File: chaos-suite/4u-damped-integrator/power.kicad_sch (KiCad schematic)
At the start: 14 parts

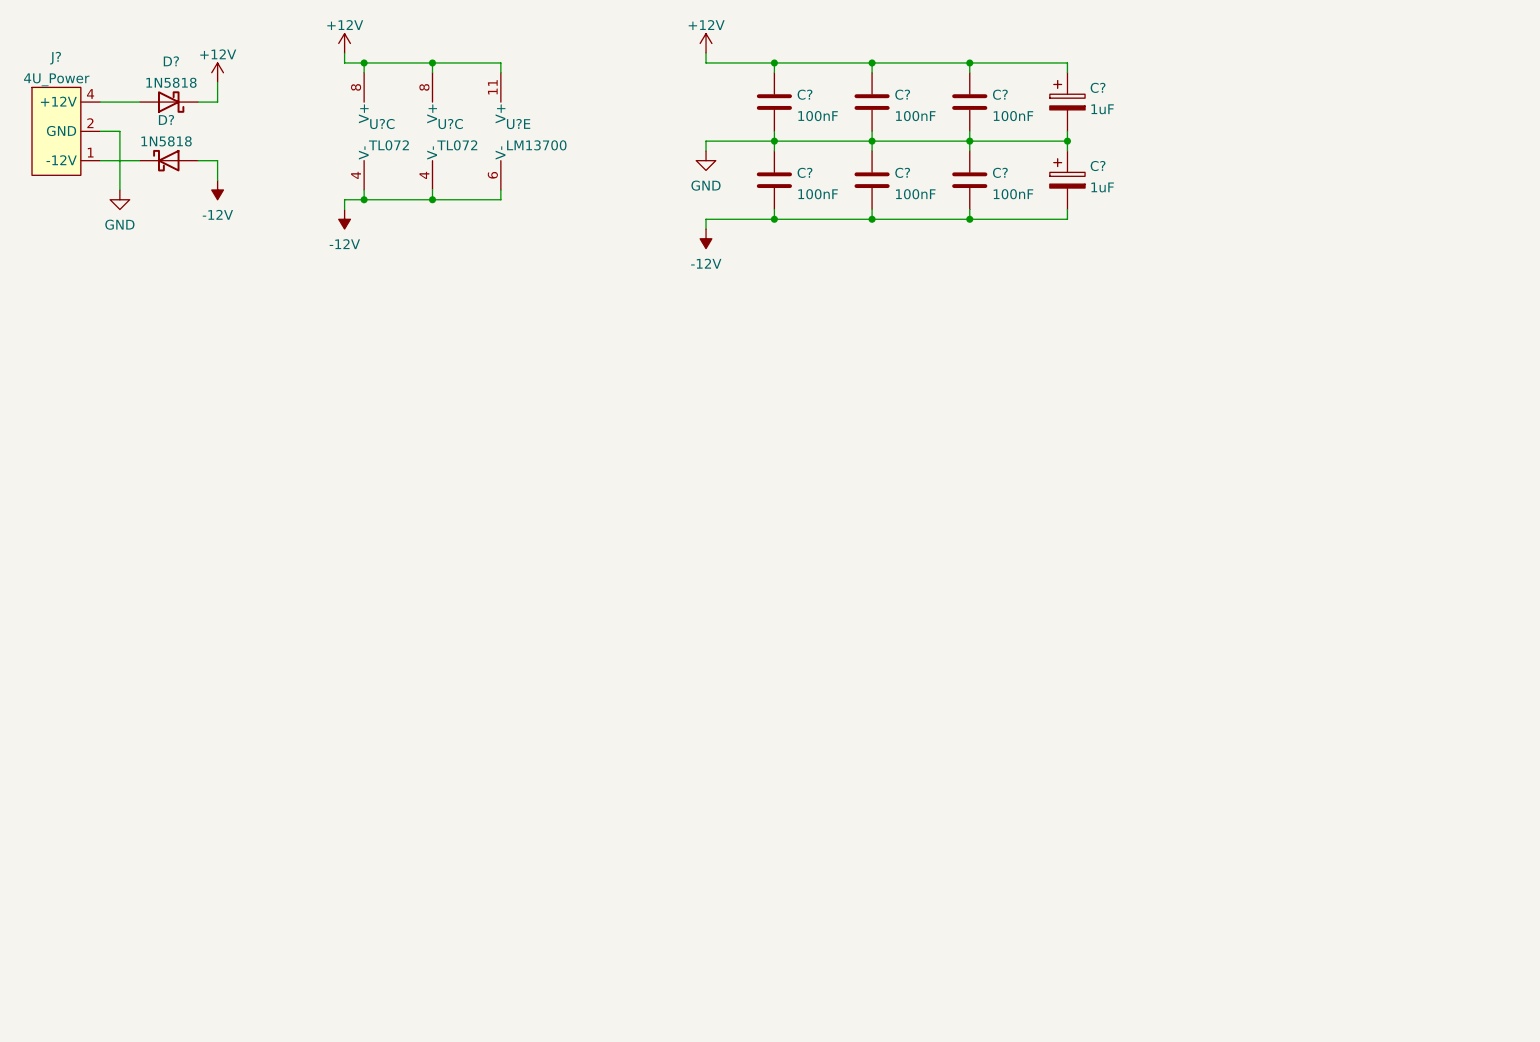
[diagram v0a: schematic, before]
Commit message: Laying out damped integrator pcb
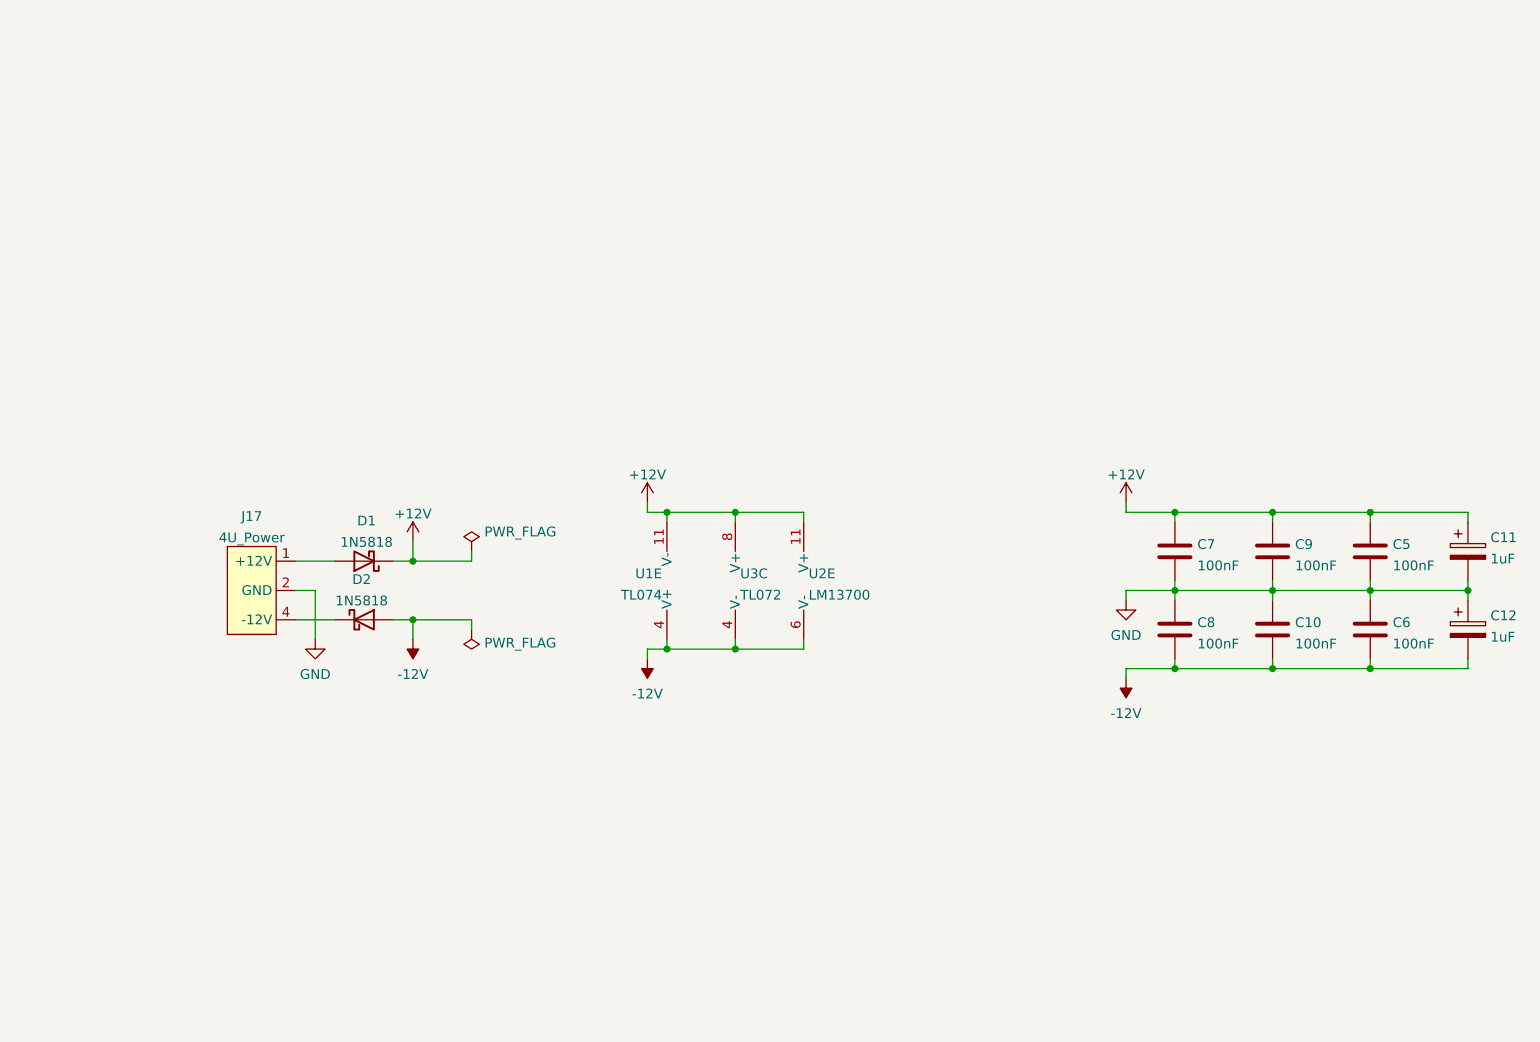
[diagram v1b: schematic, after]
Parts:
- removed C? (x2): 100nF, symbol Device:C
- removed D? (x2): 1N5818, Diode_THT:D_DO-41_SOD81_P10.16mm_Horizontal, symbol Diode:1N5818
- removed J?: 4U_Power, symbol 4U_Hardware:4U_Power
- removed U?: TL072, symbol Amplifier_Operational:TL072
- added C5, C6: 100nF, Rumblesan_Footprints:C_Rect_L7.0mm_W3.5mm_P5.00mm, symbol Device:C
- added D1: 1N5818, Rumblesan_Footprints:D_DO-41_SOD81_P10.16mm_Horizontal, symbol Diode:1N5818
- added D2: 1N5818, Rumblesan_Footprints:Diode_THT_P10.16mm_Horizontal, symbol Diode:1N5818
- added J17: 4U_Power, Rumblesan_Footprints:4u_Power_Molex_KK-254_P2.54mm, symbol 4U_Hardware:4U_Power
- added U1: TL074, Rumblesan_Footprints:DIP-14_W7.62mm_Socket, symbol Amplifier_Operational:TL074
- C10, C7, C8, C9: renamed from C?; footprint (none) -> Rumblesan_Footprints:C_Rect_L7.0mm_W3.5mm_P5.00mm
- C11, C12: renamed from C?; footprint (none) -> Capacitor_THT:CP_Radial_D5.0mm_P2.00mm
- U2: renamed from U?; footprint (none) -> Rumblesan_Footprints:DIP-16_W7.62mm_Socket
- U3: renamed from U?; footprint (none) -> Rumblesan_Footprints:DIP-8_W7.62mm_Socket
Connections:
- net +12V: now also C5.1, D1.1 (K), U1.11 (V-)
- net -12V: now also C6.2, D2.2 (A), U1.4 (V+)
- net GND: now also C5.2, C6.1, J17.2 (GND), J17.3 (GND)
- new net: D1.2 (A), J17.1 (+12V)
- new net: D2.1 (K), J17.4 (-12V)
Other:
- moved on the sheet: C10, C11, C12, C7, C8, C9, U2E, U3C

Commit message: final damped integrator tweaks
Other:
- title: (none) -> Damped Integrator
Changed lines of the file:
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@@
 (kicad_sch (version 20211123) (generator eeschema)
   (paper "A4")
+  (title_block
+    (title "Damped Integrator")
+    (date "2022-06-17")
+    (rev "r01")
+    (comment 2 "creativecommons.org/Licenses/by/4.0/")
+    (comment 3 "License: CC BY 4.0")
+    (comment 4 "Author: Guy John")
+  )
   (junction (at 97.79 96.52) (diameter 0) (color 0 0 0 0)
   )

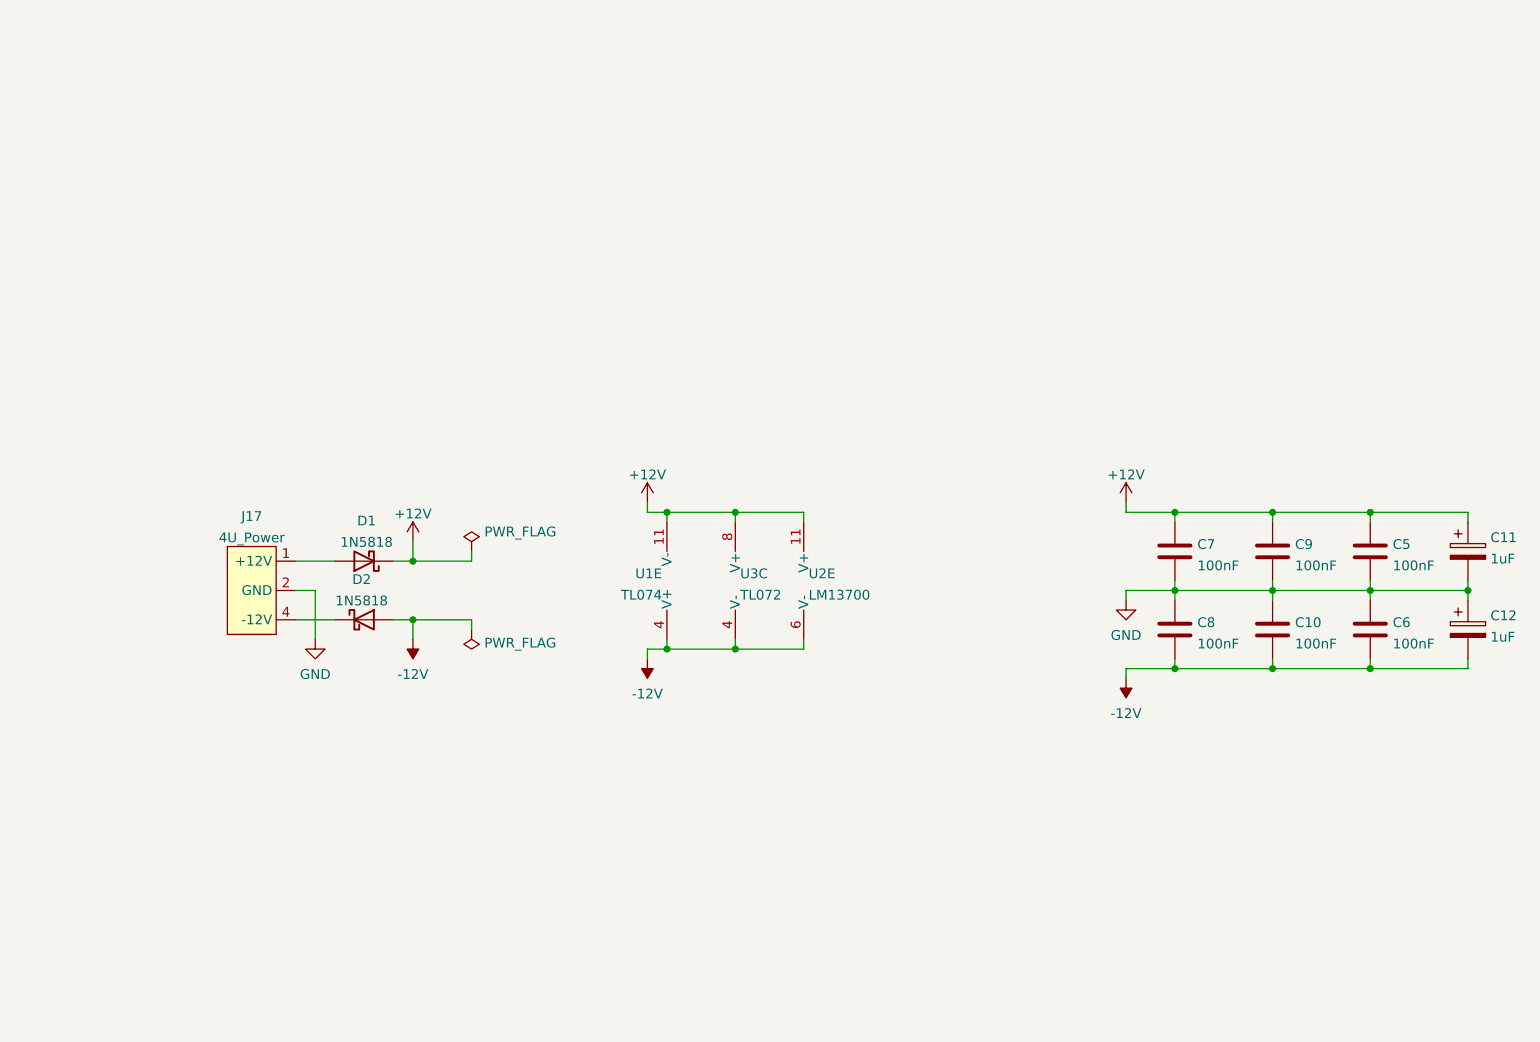
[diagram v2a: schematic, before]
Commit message: Updating damped integrator circuit and layout
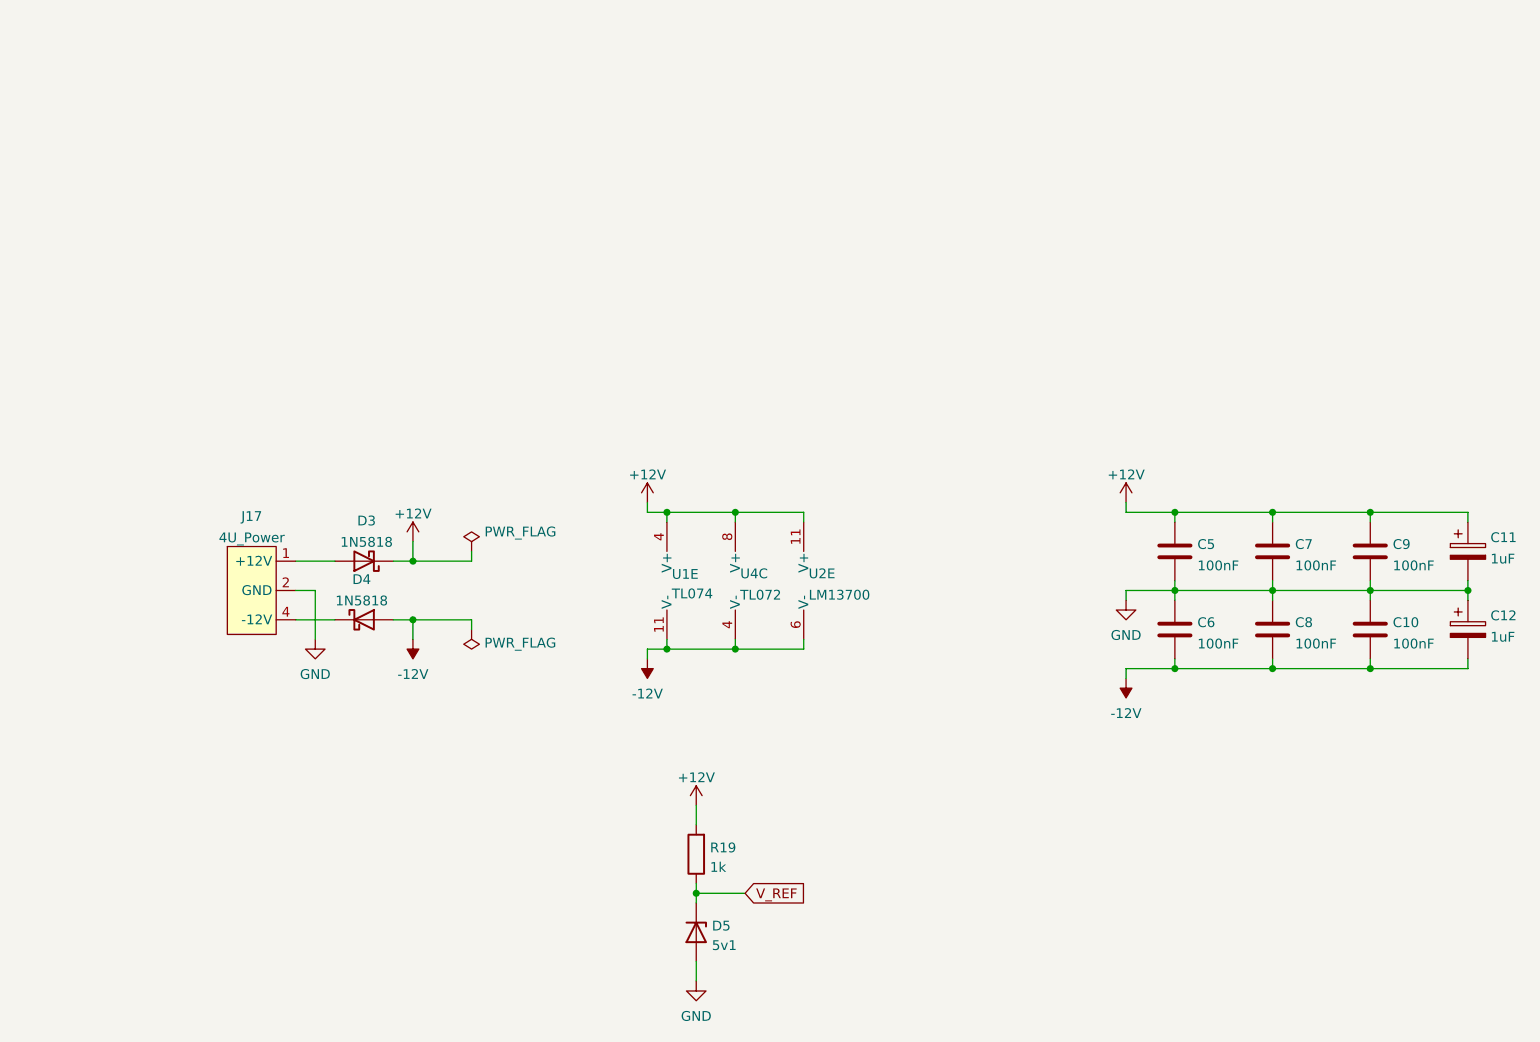
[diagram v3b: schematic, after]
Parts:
- added D5: 5v1, rumblesan-standard-parts:D_DO-35_SOD27_P7.62mm_Horizontal, symbol Device:D_Zener
- added R19: 1k, rumblesan-standard-parts:R_Axial_DIN0207_L6.3mm_D2.5mm_P10.16mm_Horizontal, symbol rumblesan-standard-parts:R
- C10: renamed from C6; footprint Rumblesan_Footprints:C_Rect_L7.0mm_W3.5mm_P5.00mm -> rumblesan-standard-parts:C_Rect_L7.0mm_W3.5mm_P5.00mm
- C11, C12: footprint Capacitor_THT:CP_Radial_D5.0mm_P2.00mm -> rumblesan-standard-parts:CP_Radial_D5.0mm_P2.00mm
- C5: renamed from C7; footprint Rumblesan_Footprints:C_Rect_L7.0mm_W3.5mm_P5.00mm -> rumblesan-standard-parts:C_Rect_L7.0mm_W3.5mm_P5.00mm
- C6: renamed from C8; footprint Rumblesan_Footprints:C_Rect_L7.0mm_W3.5mm_P5.00mm -> rumblesan-standard-parts:C_Rect_L7.0mm_W3.5mm_P5.00mm
- C7: renamed from C9; footprint Rumblesan_Footprints:C_Rect_L7.0mm_W3.5mm_P5.00mm -> rumblesan-standard-parts:C_Rect_L7.0mm_W3.5mm_P5.00mm
- C8: renamed from C10; footprint Rumblesan_Footprints:C_Rect_L7.0mm_W3.5mm_P5.00mm -> rumblesan-standard-parts:C_Rect_L7.0mm_W3.5mm_P5.00mm
- C9: renamed from C5; footprint Rumblesan_Footprints:C_Rect_L7.0mm_W3.5mm_P5.00mm -> rumblesan-standard-parts:C_Rect_L7.0mm_W3.5mm_P5.00mm
- D3: renamed from D1; footprint Rumblesan_Footprints:D_DO-41_SOD81_P10.16mm_Horizontal -> rumblesan-standard-parts:D_DO-41_SOD81_P10.16mm_Horizontal
- D4: renamed from D2; footprint Rumblesan_Footprints:Diode_THT_P10.16mm_Horizontal -> rumblesan-standard-parts:D_DO-41_SOD81_P10.16mm_Horizontal
- J17: footprint Rumblesan_Footprints:4u_Power_Molex_KK-254_P2.54mm -> 4u-power:4u_Power_Molex_KK-254_P2.54mm
- U1: footprint Rumblesan_Footprints:DIP-14_W7.62mm_Socket -> rumblesan-standard-parts:DIP-14_W7.62mm_Socket
- U2: footprint Rumblesan_Footprints:DIP-16_W7.62mm_Socket -> rumblesan-standard-parts:DIP-16_W7.62mm_Socket
- U4: renamed from U3; footprint Rumblesan_Footprints:DIP-8_W7.62mm_Socket -> rumblesan-standard-parts:DIP-8_W7.62mm_Socket
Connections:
- net +12V: now also U1.4 (V+), R19.2; no longer U1.11 (V-)
- net -12V: now also U1.11 (V-); no longer U1.4 (V+)
- net GND: now also D5.2 (A)
- new net V_REF: D5.1 (K), R19.1
